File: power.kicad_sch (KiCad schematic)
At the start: 2 parts, among them U3 TPS26400PWP, U5 TLV75733PDBV

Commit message: Nouveau convertisseur DC-DC
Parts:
- added U4: TPS62932, Package_TO_SOT_SMD:SOT-583-8, symbol Regulator_Switching:TPS62932
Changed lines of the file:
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@@
+	)
+	(symbol
+		(lib_id "Regulator_Switching:TPS62932")
+		(at 99.06 87.63 0)
+		(unit 1)
+		(body_style 1)
+		(exclude_from_sim no)
+		(in_bom yes)
+		(on_board yes)
+		(in_pos_files yes)
+		(dnp no)
+		(fields_autoplaced yes)
+		(property "Reference" "U4"
+			(at 99.06 72.39 0)
+			(show_name no)
+			(do_not_autoplace no)
+			(effects
+				(font
+					(size 1.27 1.27)
+				)
+			)
+		)
+		(property "Value" "TPS62932"
+			(at 99.06 74.93 0)
+			(show_name no)
+			(do_not_autoplace no)
+			(effects
+				(font
+					(size 1.27 1.27)
+				)
+			)
+		)
+		(property "Footprint" "Package_TO_SOT_SMD:SOT-583-8"
+			(at 99.06 113.03 0)
+			(hide yes)
+			(show_name no)
+			(do_not_autoplace no)
+			(effects
+				(font
+					(size 1.27 1.27)
+				)
+			)
+		)
+		(property "Datasheet" "https://www.ti.com/lit/ds/symlink/tps62933.pdf"
+			(at 99.06 110.49 0)
+			(hide yes)
+			(show_name no)
+			(do_not_autoplace no)
+			(effects
+				(font
+					(size 1.27 1.27)
+				)
+			)
+		)
+		(property "Description" "3.8-30V, 2A  Synchronous Buck Converters with pulse frequency modulation (PFM), SOT583-8"
+			(at 99.06 87.63 0)
+			(hide yes)
+			(show_name no)
+			(do_not_autoplace no)
+			(effects
+				(font
+					(size 1.27 1.27)
+				)
+			)
+		)
+		(pin "8"
+		)
+		(pin "6"
+		)
+		(pin "5"
+		)
+		(pin "2"
+		)
+		(pin "4"
+		)
+		(pin "1"
+		)
+		(pin "7"
+		)
+		(pin "3"
+		)
+		(instances
+			(project "analog2can"
+				(path "/83888944-f662-44d6-9bff-94055f87dd66/1a63739b-49c7-4b8a-8b5c-65c9fea63203"
+					(reference "U4")
+					(unit 1)
+				)
+			)
+		)
 	)
 	(symbol

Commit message: no change yes?
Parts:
- removed U3: TPS26400PWP, Package_DFN_QFN:Texas_RHF0024A_VQFN-24-1EP_4x5mm_P0.5mm_EP2.65x3.65mm_ThermalVias, symbol Power_Management:TPS26400PWP
- added U6: TPS26400PWP, Package_SO:HTSSOP-16-1EP_4.4x5mm_P0.65mm_EP3.4x5mm_Mask2.66x2.46mm_ThermalVias, symbol Power_Management:TPS26400PWP
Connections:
- new net: U6.1 (IN), U6.2 (IN)
- new net: U6.15 (OUT), U6.16 (OUT)
- new net: U6.17 (RTN), U6.8 (RTN)
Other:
- moved on the sheet: U4, U5
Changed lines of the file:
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@@
 	(paper "A4")
 	(symbol
-		(lib_id "Power_Management:TPS26400PWP")
-		(at 173.99 59.69 0)
-		(unit 1)
-		(body_style 1)
-		(exclude_from_sim no)
-		(in_bom yes)
-		(on_board yes)
-		(in_pos_files yes)
-		(dnp no)
-		(fields_autoplaced yes)
-		(property "Reference" "U3"
-			(at 173.99 39.37 0)
-			(show_name no)
-			(do_not_autoplace no)
-			(effects
-				(font
-					(size 1.27 1.27)
-				)
-			)
-		)
-		(property "Value" "TPS26400PWP"
-			(at 173.99 41.91 0)
-			(show_name no)
-			(do_not_autoplace no)
-			(effects
-				(font
-					(size 1.27 1.27)
-				)
-			)
-		)
-		(property "Footprint" "Package_DFN_QFN:Texas_RHF0024A_VQFN-24-1EP_4x5mm_P0.5mm_EP2.65x3.65mm_ThermalVias"
-			(at 173.99 90.17 0)
-			(hide yes)
-			(show_name no)
-			(do_not_autoplace no)
-			(effects
-				(font
-					(size 1.27 1.27)
-				)
-			)
-		)
-		(property "Datasheet" "https://www.ti.com/lit/ds/symlink/tps2640.pdf"
-			(at 173.99 92.71 0)
-			(hide yes)
-			(show_name no)
-			(do_not_autoplace no)
-			(effects
-				(font
-					(size 1.27 1.27)
-				)
-			)
-		)
-		(property "Description" "42V, 2A Current Limiting, Industrial eFuse, Reverse Current Blocking, Adjustable Overvoltage cut-off, Active Current Limiting, Circuit Breaker with auto-retry, HTSSOP-16"
-			(at 173.99 38.1 0)
-			(hide yes)
-			(show_name no)
-			(do_not_autoplace no)
-			(effects
-				(font
-					(size 1.27 1.27)
-				)
-			)
-		)
-		(pin "7"
-		)
-		(pin "6"
-		)
-		(pin "2"
-		)
-		(pin "4"
-		)
-		(pin "3"
-		)
-		(pin "13"
-		)
-		(pin "5"
-		)
-		(pin "8"
-		)
-		(pin "14"
-		)
-		(pin "10"
-		)
-		(pin "12"
-		)
-		(pin "9"
-		)
-		(pin "17"
-		)
-		(pin "1"
-		)
-		(pin "15"
-		)
-		(pin "11"
-		)
-		(pin "16"
-		)
-		(instances
-			(project "analog2can"
-				(path "/83888944-f662-44d6-9bff-94055f87dd66/1a63739b-49c7-4b8a-8b5c-65c9fea63203"
-					(reference "U3")
-					(unit 1)
-				)
-			)
-		)
-	)
-	(symbol
 		(lib_id "Regulator_Switching:TPS62932")
-		(at 99.06 87.63 0)
+		(at 166.37 151.13 0)
 		(unit 1)
 		(body_style 1)
@@
 		(fields_autoplaced yes)
 		(property "Reference" "U4"
-			(at 99.06 72.39 0)
+			(at 166.37 135.89 0)
 			(show_name no)
 			(do_not_autoplace no)
@@
 		)
 		(property "Value" "TPS62932"
-			(at 99.06 74.93 0)
+			(at 166.37 138.43 0)
 			(show_name no)
 			(do_not_autoplace no)
@@
 		)
 		(property "Footprint" "Package_TO_SOT_SMD:SOT-583-8"
-			(at 99.06 113.03 0)
+			(at 166.37 176.53 0)
 			(hide yes)
 			(show_name no)
@@
 		)
 		(property "Datasheet" "https://www.ti.com/lit/ds/symlink/tps62933.pdf"
-			(at 99.06 110.49 0)
+			(at 166.37 173.99 0)
 			(hide yes)
 			(show_name no)
@@
 		)
 		(property "Description" "3.8-30V, 2A  Synchronous Buck Converters with pulse frequency modulation (PFM), SOT583-8"
-			(at 99.06 87.63 0)
+			(at 166.37 151.13 0)
 			(hide yes)
 			(show_name no)
@@
 	)
 	(symbol
+		(lib_id "Power_Management:TPS26400PWP")
+		(at 83.82 55.88 0)
+		(unit 1)
+		(body_style 1)
+		(exclude_from_sim no)
+		(in_bom yes)
+		(on_board yes)
+		(in_pos_files yes)
+		(dnp no)
+		(fields_autoplaced yes)
+		(property "Reference" "U6"
+			(at 83.82 35.56 0)
+			(show_name no)
+			(do_not_autoplace no)
+			(effects
+				(font
+					(size 1.27 1.27)
+				)
+			)
+		)
+		(property "Value" "TPS26400PWP"
+			(at 83.82 38.1 0)
+			(show_name no)
+			(do_not_autoplace no)
+			(effects
+				(font
+					(size 1.27 1.27)
+				)
+			)
+		)
+		(property "Footprint" "Package_SO:HTSSOP-16-1EP_4.4x5mm_P0.65mm_EP3.4x5mm_Mask2.66x2.46mm_ThermalVias"
+			(at 83.82 86.36 0)
+			(hide yes)
+			(show_name no)
+			(do_not_autoplace no)
+			(effects
+				(font
+					(size 1.27 1.27)
+				)
+			)
+		)
+		(property "Datasheet" "https://www.ti.com/lit/ds/symlink/tps2640.pdf"
+			(at 83.82 88.9 0)
+			(hide yes)
+			(show_name no)
+			(do_not_autoplace no)
+			(effects
+				(font
+					(size 1.27 1.27)
+				)
+			)
+		)
+		(property "Description" "42V, 2A Current Limiting, Industrial eFuse, Reverse Current Blocking, Adjustable Overvoltage cut-off, Active Current Limiting, Circuit Breaker with auto-retry, HTSSOP-16"
+			(at 83.82 34.29 0)
+			(hide yes)
+			(show_name no)
+			(do_not_autoplace no)
+			(effects
+				(font
+					(size 1.27 1.27)
+				)
+			)
+		)
+		(pin "2"
+		)
+		(pin "13"
+		)
+		(pin "5"
+		)
+		(pin "9"
+		)
+		(pin "14"
+		)
+		(pin "1"
+		)
+		(pin "8"
+		)
+		(pin "12"
+		)
+		(pin "3"
+		)
+		(pin "7"
+		)
+		(pin "10"
+		)
+		(pin "4"
+		)
+		(pin "11"
+		)
+		(pin "15"
+		)
+		(pin "17"
+		)
+		(pin "16"
+		)
+		(pin "6"
+		)
+		(instances
+			(project "analog2can"
+				(path "/83888944-f662-44d6-9bff-94055f87dd66/1a63739b-49c7-4b8a-8b5c-65c9fea63203"
+					(reference "U6")
+					(unit 1)
+				)
+			)
+		)
+	)
+	(symbol
 		(lib_id "Regulator_Linear:TLV75733PDBV")
-		(at 143.51 53.34 0)
+		(at 210.82 116.84 0)
 		(unit 1)
 		(body_style 1)
@@
 		(fields_autoplaced yes)
 		(property "Reference" "U5"
-			(at 143.51 44.45 0)
+			(at 210.82 107.95 0)
 			(show_name no)
 			(do_not_autoplace no)
@@
 		)
 		(property "Value" "TLV75733PDBV"
-			(at 143.51 46.99 0)
+			(at 210.82 110.49 0)
 			(show_name no)
 			(do_not_autoplace no)
@@
 		)
 		(property "Footprint" "Package_TO_SOT_SMD:SOT-223-3_TabPin2"
-			(at 143.51 45.085 0)
+			(at 210.82 108.585 0)
 			(hide yes)
 			(show_name no)
@@
 		)
 		(property "Datasheet" "https://www.ti.com/lit/ds/symlink/tlv757p.pdf"
-			(at 143.51 52.07 0)
+			(at 210.82 115.57 0)
 			(hide yes)
 			(show_name no)
@@
 		)
 		(property "Description" "1A Low IQ Small Size Low Dropout Voltage Regulator, Fixed Output 3.3V, SOT-23-5"
-			(at 143.51 53.34 0)
-			(hide yes)
-			(show_name no)
+			(at 210.82 116.84 0)
+			(hide yes)
+			(show_name no)

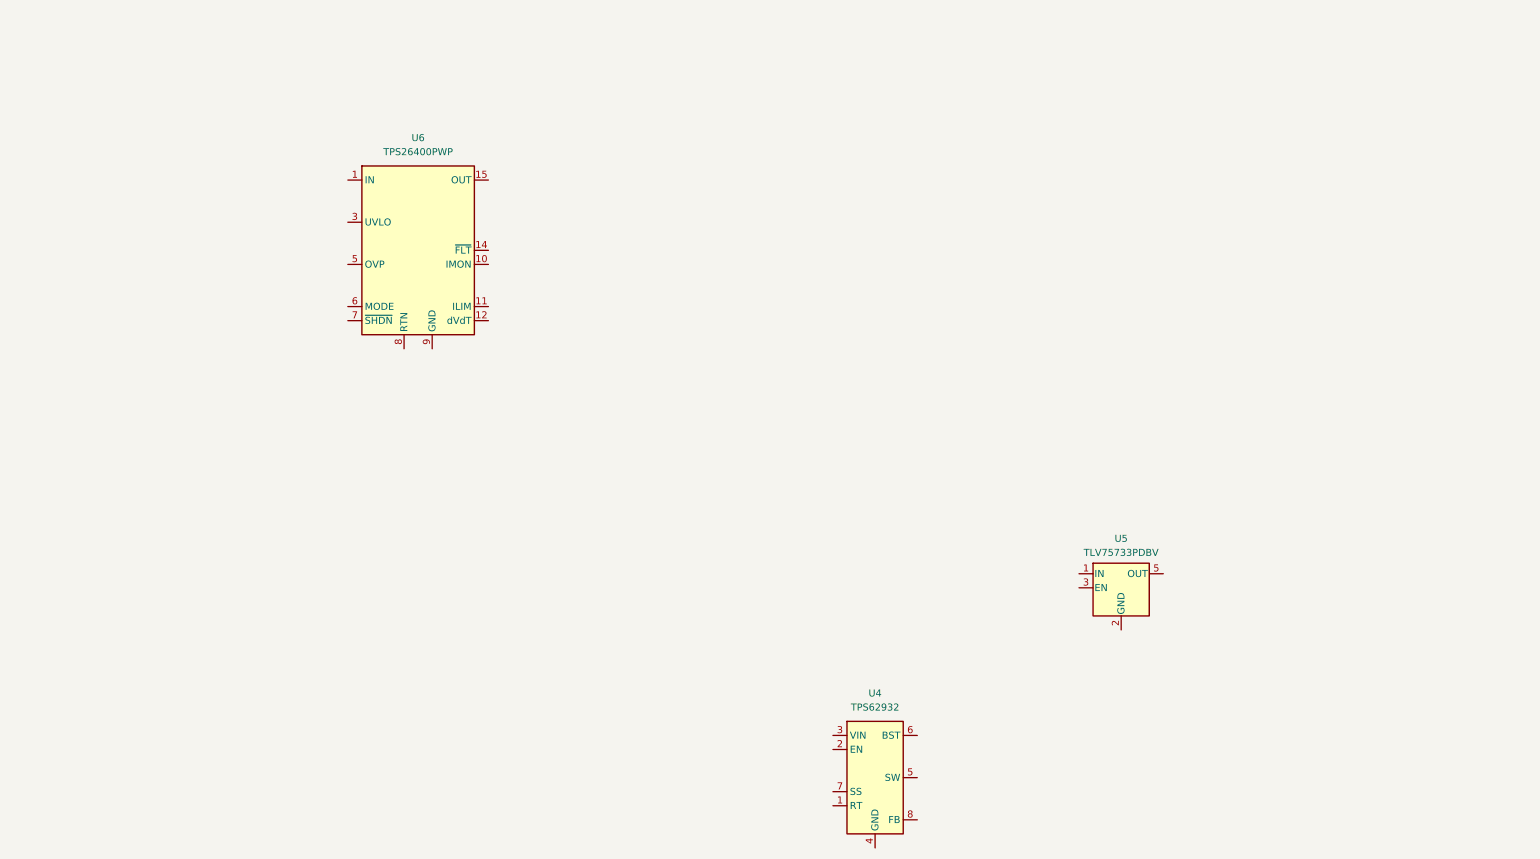
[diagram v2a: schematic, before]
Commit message: Power supply done, need to do comm, analog and logic
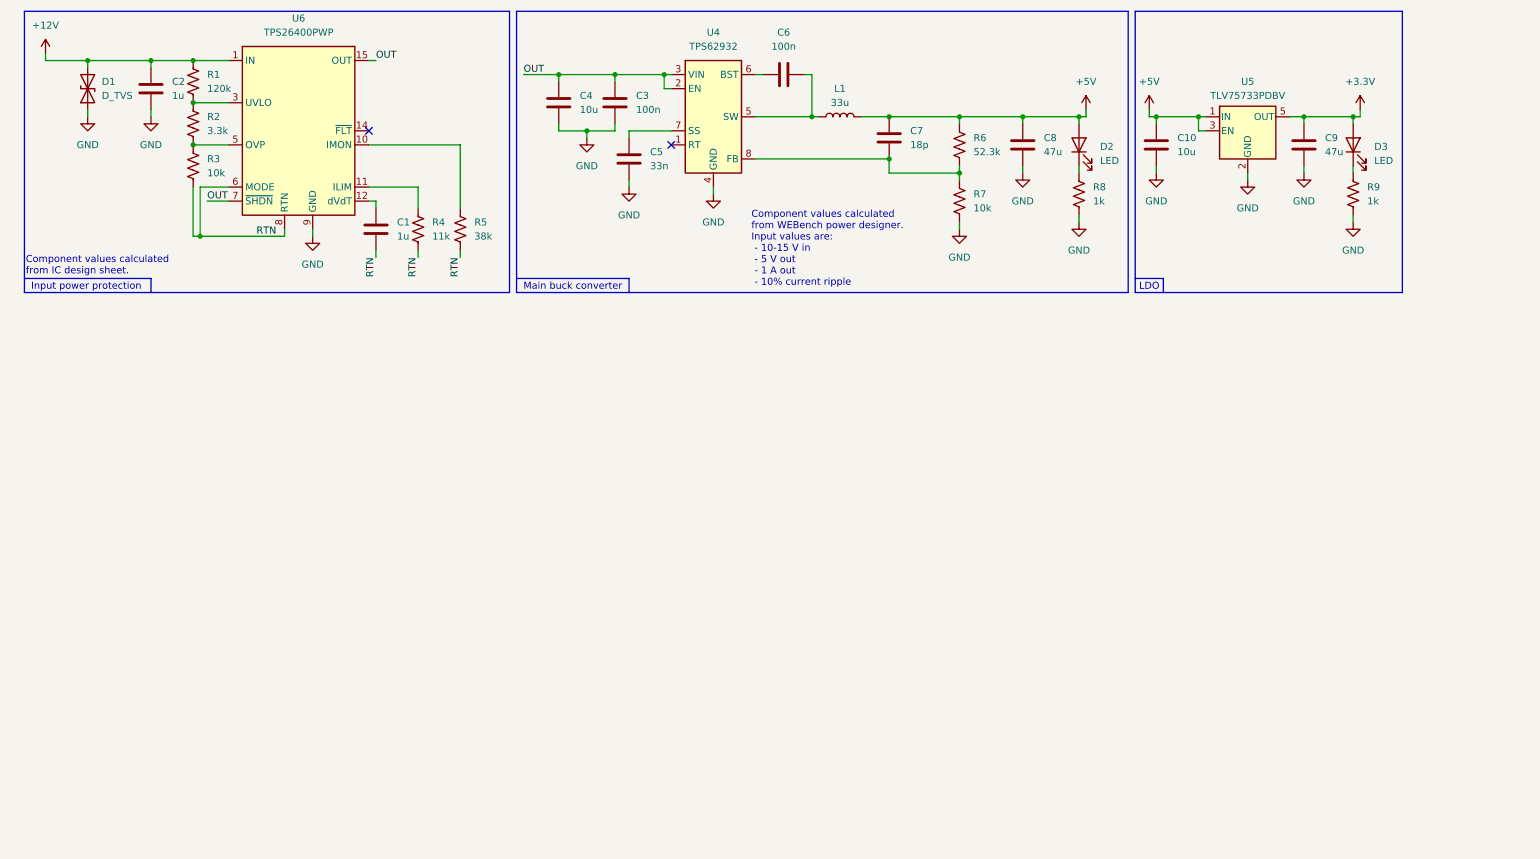
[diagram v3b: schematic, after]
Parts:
- added C1, C2: 1u, symbol Device:C
- added C10, C4: 10u, symbol Device:C
- added C3, C6: 100n, symbol Device:C
- added C5: 33n, symbol Device:C
- added C7: 18p, symbol Device:C
- added C8, C9: 47u, symbol Device:C
- added D1: D_TVS, symbol Device:D_TVS
- added D2, D3: LED, symbol Device:LED
- added L1: 33u, symbol Device:L
- added R1: 120k, symbol Device:R_US
- added R2: 3.3k, symbol Device:R_US
- added R3, R7: 10k, symbol Device:R_US
- added R4: 11k, symbol Device:R_US
- added R5: 38k, symbol Device:R_US
- added R6: 52.3k, symbol Device:R_US
- added R8, R9: 1k, symbol Device:R_US
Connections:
- net OUT: now reaches U4.2 (EN)
- net OUT: now also U4.3 (VIN), U6.15 (OUT), U6.16 (OUT), U6.7 (~{SHDN}), C3.1, C4.1
- net GND: now reaches U4.4 (GND)
- net GND: now also U5.2 (GND), U6.9 (GND), C10.2, C2.2, C3.2, C4.2, C5.2, C8.2, C9.2, D1.1 (A1), R7.2, R8.2, R9.2
- net at U4.5 (SW): now also C6.2, L1.1
- net at U4.6 (BST): now also C6.1
- net at U4.7 (SS): now also C5.1
- net at U4.8 (FB): now also C7.1, R6.2, R7.1
- net +12V: now reaches U6.1 (IN), U6.2 (IN)
- net +12V: now also C2.1, D1.2 (A2), R1.1
- net at U6.10 (IMON): now also R5.1
- net at U6.11 (ILIM): now also R4.1
- net at U6.12 (dVdT): now also C1.1
- net RTN: now reaches U6.17 (RTN), U6.8 (RTN)
- net RTN: now also U6.6 (MODE), C1.2, R3.2, R4.2, R5.2
- net at U6.3 (UVLO): now also R1.2, R2.1
- net at U6.5 (OVP): now also R2.2, R3.1
- net +5V: now reaches U5.1 (IN)
- net +5V: now also U5.3 (EN), C10.1, C7.2, C8.1, D2.2 (A), L1.2, R6.1
- net +3.3V: now reaches U5.5 (OUT)
- net +3.3V: now also C9.1, D3.2 (A)
- new net: D2.1 (K), R8.1
- new net: D3.1 (K), R9.1
- no-connect marks 0 -> 2
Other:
- note added: "Component values calculated from IC design sheet."
- note added: "Component values calculated from WEBench power designer. Input values are: - 10-15 V in - 5 V out - 1 A out - 10% current ripple"
- note added: "Input power protection"
- note added: "LDO"
- note added: "Main buck converter"
- moved on the sheet: U4, U5, U6

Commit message: Schema devrait etre fini. A revalider avec le layout (Surtout SWO pour debug)
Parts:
- removed C9: 47u, symbol Device:C
- removed D1: D_TVS, symbol Device:D_TVS
- added C18, C20, C22, C23: 15u, Capacitor_SMD:C_0805_2012Metric_Pad1.18x1.45mm_HandSolder, symbol Device:C
- added D8: D_Zener, Diode_SMD:D_SOD-523, symbol Device:D_Zener
- C11: renamed from C2; footprint (none) -> Capacitor_SMD:C_0603_1608Metric_Pad1.08x0.95mm_HandSolder
- C12: renamed from C1; footprint (none) -> Capacitor_SMD:C_0603_1608Metric_Pad1.08x0.95mm_HandSolder
- C13: renamed from C4; footprint (none) -> LED_SMD:LED_0805_2012Metric_Pad1.15x1.40mm_HandSolder
- C14: renamed from C3; value 100n -> 0.1u; footprint (none) -> Capacitor_SMD:C_0603_1608Metric_Pad1.08x0.95mm_HandSolder
- C15: renamed from C5; footprint (none) -> Capacitor_SMD:C_0402_1005Metric_Pad0.74x0.62mm_HandSolder
- C16: renamed from C6; footprint (none) -> Capacitor_SMD:C_0402_1005Metric_Pad0.74x0.62mm_HandSolder
- C17: renamed from C7; footprint (none) -> Capacitor_SMD:C_0402_1005Metric_Pad0.74x0.62mm_HandSolder
- C19: renamed from C8; value 47u -> 15u; footprint (none) -> Capacitor_SMD:C_0805_2012Metric_Pad1.18x1.45mm_HandSolder
- C21: renamed from C10; footprint (none) -> Capacitor_SMD:C_0805_2012Metric_Pad1.18x1.45mm_HandSolder
- D10: renamed from D3; footprint (none) -> LED_SMD:LED_0603_1608Metric_Pad1.05x0.95mm_HandSolder
- D9: renamed from D2; footprint (none) -> LED_SMD:LED_0603_1608Metric_Pad1.05x0.95mm_HandSolder
- L1: footprint (none) -> Inductor_SMD:L_Vishay_IHLP-6767
- R13: renamed from R1; footprint (none) -> Resistor_SMD:R_0603_1608Metric_Pad0.98x0.95mm_HandSolder
- R14: renamed from R2; footprint (none) -> Resistor_SMD:R_0603_1608Metric_Pad0.98x0.95mm_HandSolder
- R15: renamed from R3; footprint (none) -> Resistor_SMD:R_0603_1608Metric_Pad0.98x0.95mm_HandSolder
- R16: renamed from R4; footprint (none) -> Resistor_SMD:R_0603_1608Metric_Pad0.98x0.95mm_HandSolder
- R17: renamed from R5; footprint (none) -> Resistor_SMD:R_0603_1608Metric_Pad0.98x0.95mm_HandSolder
- R18: renamed from R6; footprint (none) -> Resistor_SMD:R_0603_1608Metric_Pad0.98x0.95mm_HandSolder
- R19: renamed from R7; footprint (none) -> Resistor_SMD:R_0603_1608Metric_Pad0.98x0.95mm_HandSolder
- R20: renamed from R8; footprint (none) -> Resistor_SMD:R_0603_1608Metric_Pad0.98x0.95mm_HandSolder
- R21: renamed from R9; footprint (none) -> Resistor_SMD:R_0603_1608Metric_Pad0.98x0.95mm_HandSolder
- renumbered U6 to U3
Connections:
- net +12V: now also D8.1 (K)
- net +3.3V: now also C22.1, C23.1
- net +5V: now also C18.1, C20.1
- net GND: now also C18.2, C20.2, C22.2, C23.2, D8.2 (A)
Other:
- moved on the sheet: C17, C19, C21, D10, D9, R18, R19, R20, R21, U5

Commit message: Debut layout PCB et review Schema done
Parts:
- U5: footprint Package_TO_SOT_SMD:SOT-223-3_TabPin2 -> Package_TO_SOT_SMD:SOT-23-5
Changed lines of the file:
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@@
 			)
 		)
-		(property "Footprint" "Package_TO_SOT_SMD:SOT-223-3_TabPin2"
+		(property "Footprint" "Package_TO_SOT_SMD:SOT-23-5"
 			(at 243.84 26.035 0)
 			(hide yes)

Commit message: Fin layout buck, debut layout efuse
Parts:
- L1: footprint Inductor_SMD:L_Vishay_IHLP-6767 -> Inductor_SMD:L_Coilcraft_XAL1510-333
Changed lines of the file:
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@@
 			)
 		)
-		(property "Footprint" "Inductor_SMD:L_Vishay_IHLP-6767"
+		(property "Footprint" "Inductor_SMD:L_Coilcraft_XAL1510-333"
 			(at 160.02 31.75 0)
 			(hide yes)
